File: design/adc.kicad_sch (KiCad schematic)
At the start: 26 parts, among them J6 JUMPER_DFS/GAIN, U11 TLV431ACDBZR, U12 AD9214

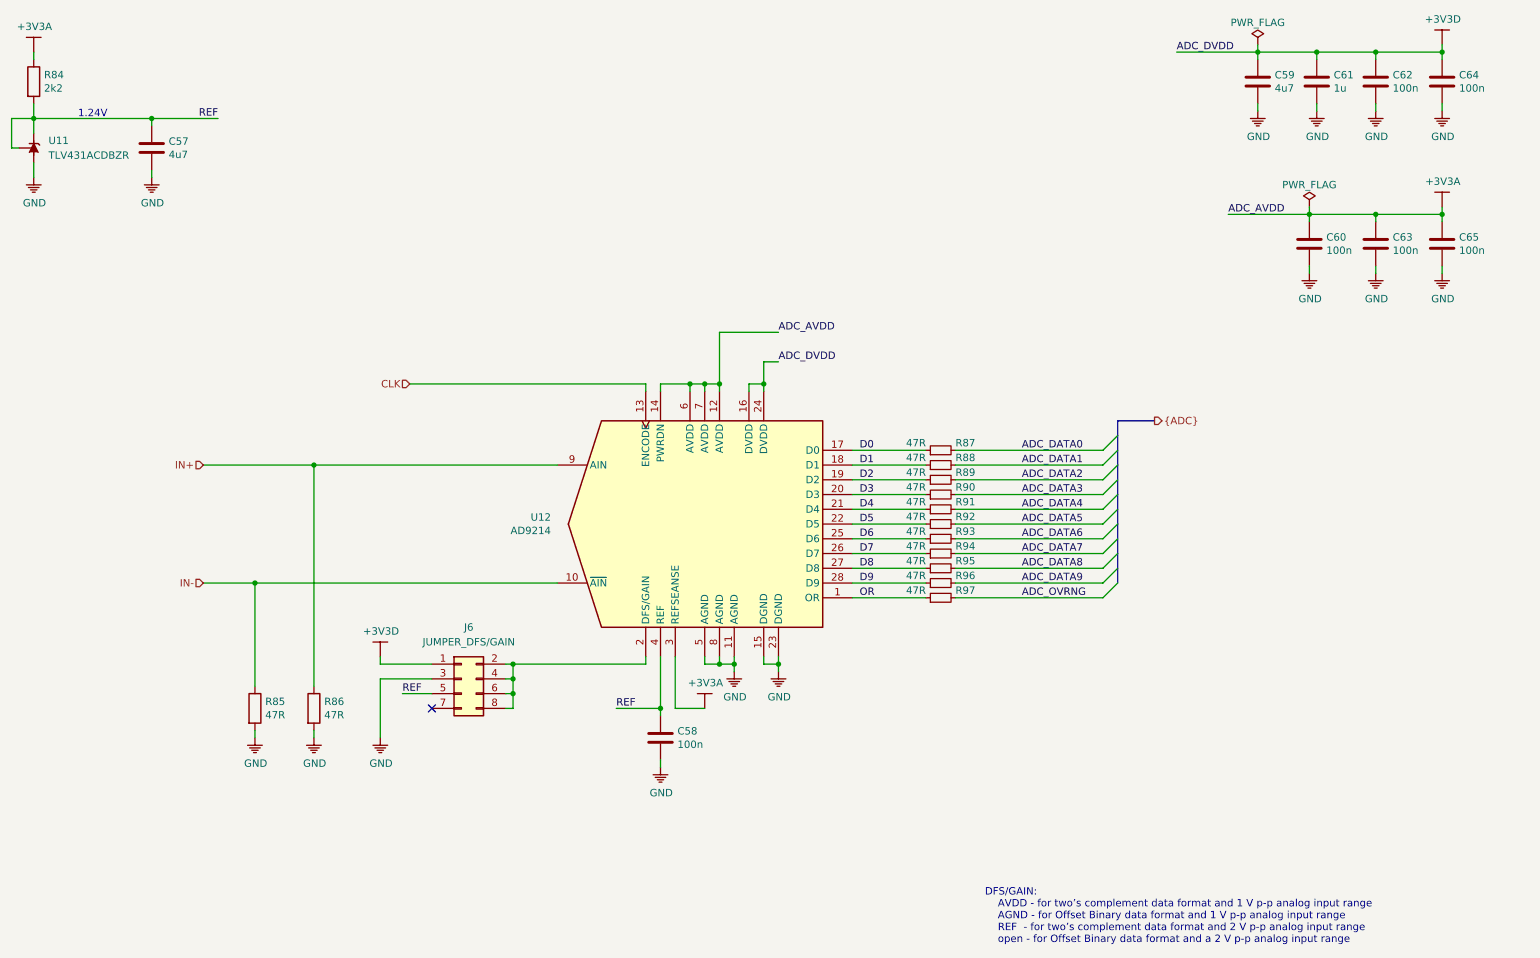
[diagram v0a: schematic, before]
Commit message: Added ADC placement
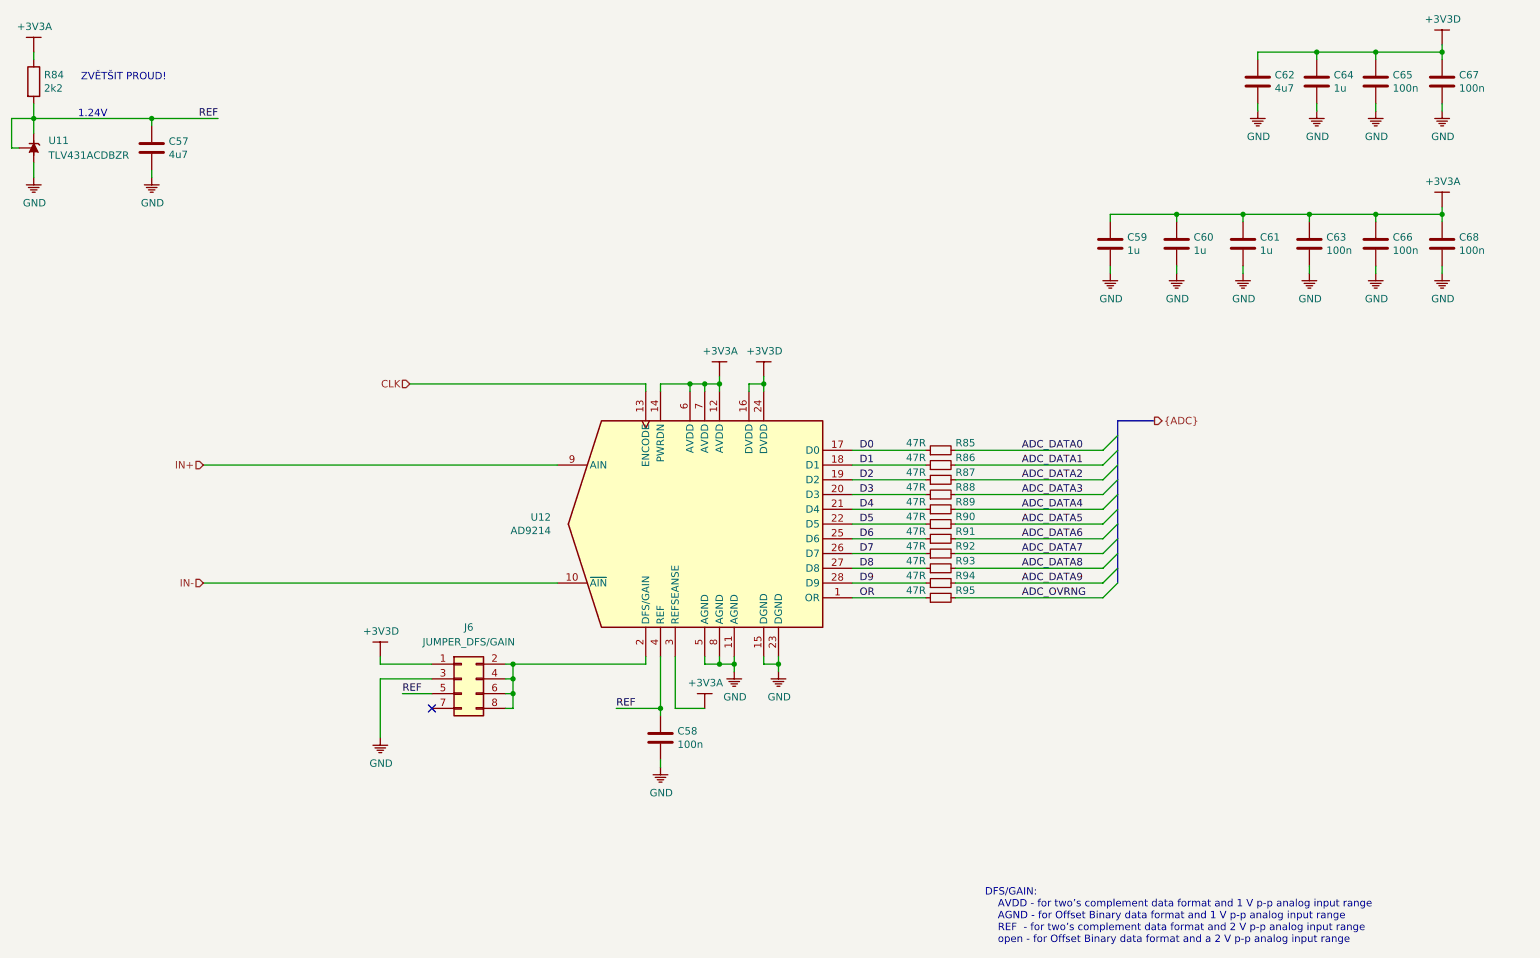
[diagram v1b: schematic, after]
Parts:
- removed R85, R86: 47R, Resistor_SMD:R_0402_1005Metric, symbol Device:R
- added C59, C60, C61: 1u, Capacitor_SMD:C_0402_1005Metric, symbol Device:C
- renumbered C59 to C62, C60 to C63, C61 to C64, C62 to C65, C63 to C66, C64 to C67, C65 to C68, R87 to R85, R88 to R86, R89 to R87, R90 to R88, R91 to R89, R92 to R90, R93 to R91, R94 to R92, R95 to R93, R96 to R94, R97 to R95
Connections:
- net +3V3A: now also C59.1, C60.1, C61.1
- net GND: now also C59.2, C60.2, C61.2
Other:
- note added: "ZVĚTŠIT PROUD!"

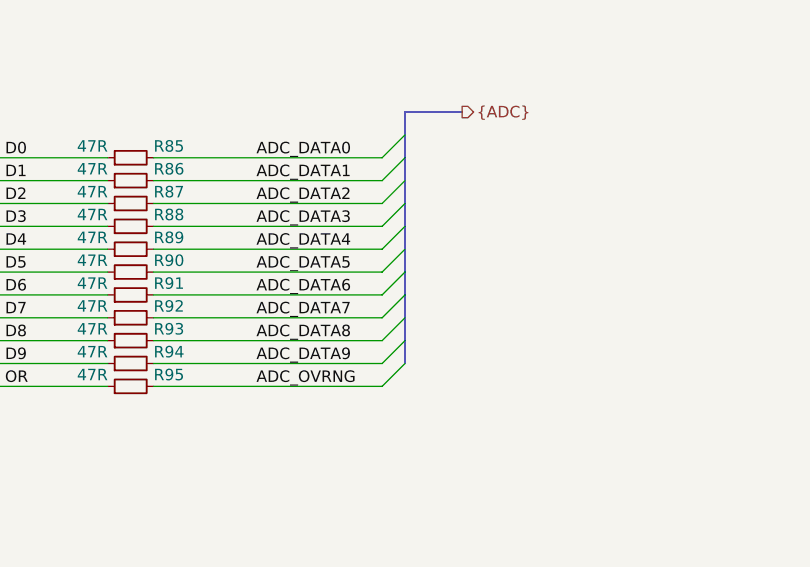
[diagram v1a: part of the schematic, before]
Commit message: Fixed LNA power
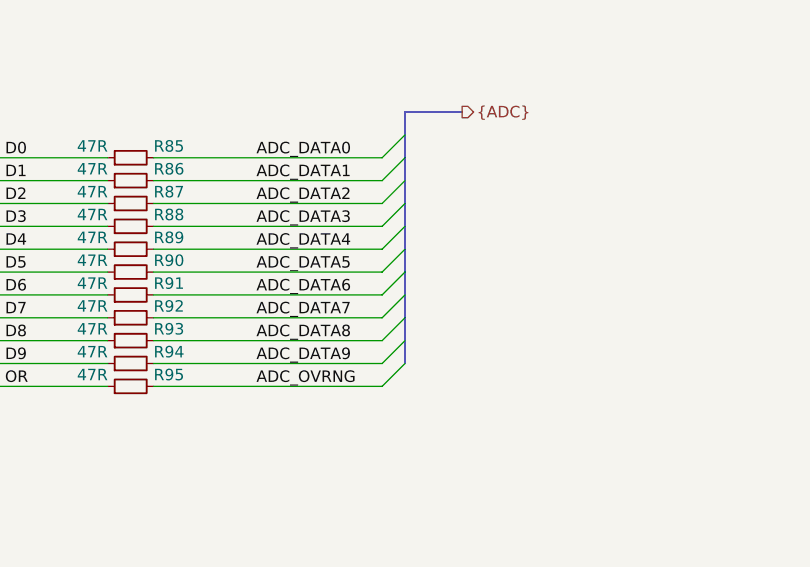
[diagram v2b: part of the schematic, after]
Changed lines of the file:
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@@
-(kicad_sch (version 20200310) (host eeschema "5.99.0-unknown-5cf474e~101~ubuntu18.04.1")
+(kicad_sch (version 20200506) (host eeschema "5.99.0-unknown-1f9723c~101~ubuntu18.04.1")
   (page "A4")
   (title_block
@@
     (company "Jan Vykydal")
   )
+  (junction (at 153.67 82.55))
+  (junction (at 110.49 130.81))
+  (junction (at 110.49 135.89))
+  (junction (at 248.92 25.4))
+  (junction (at 236.22 53.34))
+  (junction (at 148.59 130.81))
+  (junction (at 270.51 53.34))
+  (junction (at 140.97 82.55))
   (junction (at 247.65 53.34))
-  (junction (at 110.49 130.81))
+  (junction (at 27.94 36.83))
+  (junction (at 224.79 53.34))
+  (junction (at 156.21 130.81))
+  (junction (at 259.08 53.34))
+  (junction (at 135.89 138.43))
   (junction (at 48.26 36.83))
-  (junction (at 236.22 53.34))
-  (junction (at 110.49 135.89))
-  (junction (at 270.51 25.4))
-  (junction (at 224.79 53.34))
-  (junction (at 140.97 82.55))
-  (junction (at 259.08 53.34))
-  (junction (at 153.67 82.55))
   (junction (at 259.08 25.4))
-  (junction (at 143.51 82.55))
   (junction (at 146.05 82.55))
-  (junction (at 248.92 25.4))
-  (junction (at 270.51 53.34))
-  (junction (at 148.59 130.81))
   (junction (at 110.49 133.35))
   (junction (at 146.05 130.81))
-  (junction (at 27.94 36.83))
-  (junction (at 135.89 138.43))
-  (junction (at 156.21 130.81))
+  (junction (at 143.51 82.55))
+  (junction (at 270.51 25.4))
   (no_connect (at 96.52 138.43))
   (bus_entry (at 212.09 93.98) (size 2.54 -2.54))
@@
   (bus (pts (xy 214.63 88.9) (xy 214.63 93.98)))
   (bus (pts (xy 214.63 93.98) (xy 214.63 99.06)))
-  (bus (pts (xy 214.63 99.06) (xy 214.63 101.6)))
-  (bus (pts (xy 214.63 101.6) (xy 214.63 106.68)))
-  (bus (pts (xy 214.63 106.68) (xy 214.63 109.22)))
-  (bus (pts (xy 214.63 109.22) (xy 214.63 114.3)))
-  (bus (pts (xy 214.63 114.3) (xy 214.63 116.84)))
+  (bus (pts (xy 214.63 99.06) (xy 214.63 104.14)))
+  (bus (pts (xy 214.63 104.14) (xy 214.63 106.68)))
+  (bus (pts (xy 214.63 106.68) (xy 214.63 111.76)))
+  (bus (pts (xy 214.63 111.76) (xy 214.63 116.84)))
   (bus (pts (xy 220.98 88.9) (xy 214.63 88.9)))
   (text "1.24V" (at 40.64 36.83 180)

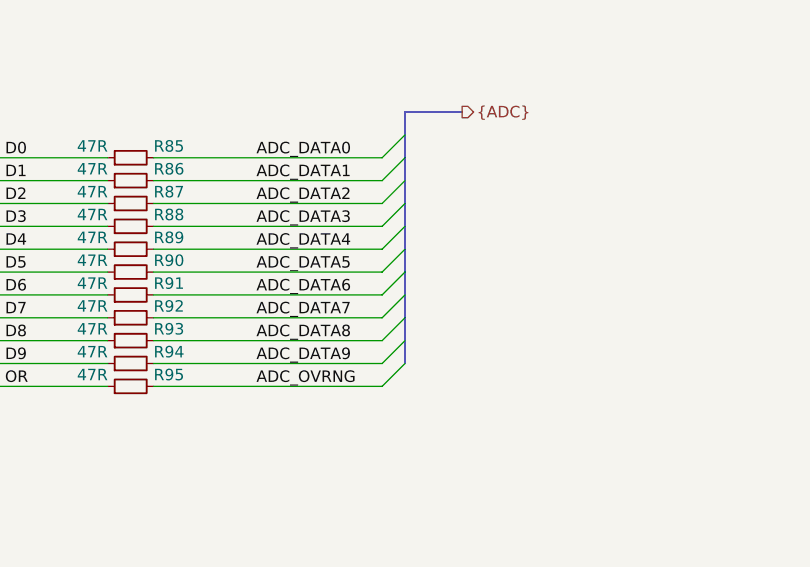
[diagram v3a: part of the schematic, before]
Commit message: Added buses that were removed when converting from the old format
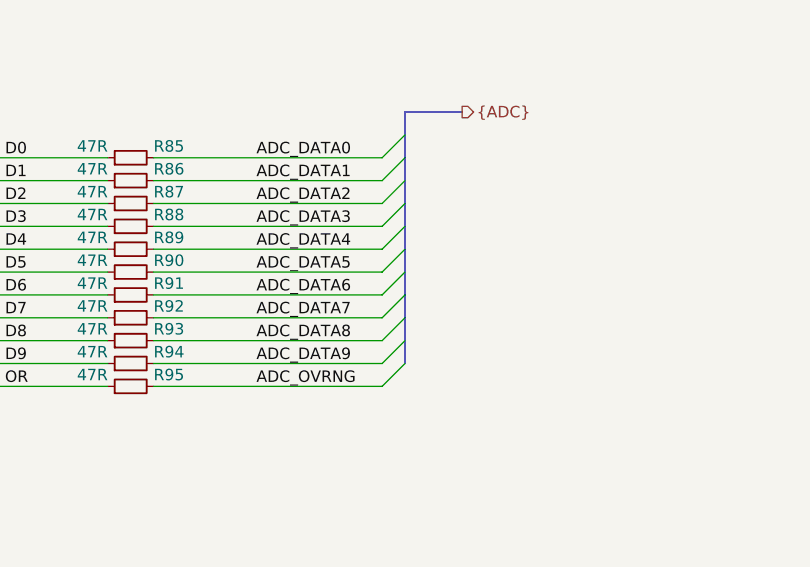
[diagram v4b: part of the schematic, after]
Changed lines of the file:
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@@
     (company "Jan Vykydal")
   )
+  (bus_alias "ADC" (members "ADC_DATA[9..0]" "ADC_OVRNG"))
+  (junction (at 146.05 82.55))
+  (junction (at 143.51 82.55))
+  (junction (at 156.21 130.81))
+  (junction (at 270.51 25.4))
+  (junction (at 146.05 130.81))
+  (junction (at 140.97 82.55))
+  (junction (at 259.08 53.34))
+  (junction (at 259.08 25.4))
+  (junction (at 110.49 130.81))
+  (junction (at 224.79 53.34))
+  (junction (at 248.92 25.4))
+  (junction (at 135.89 138.43))
+  (junction (at 48.26 36.83))
   (junction (at 153.67 82.55))
-  (junction (at 110.49 130.81))
-  (junction (at 110.49 135.89))
-  (junction (at 248.92 25.4))
   (junction (at 236.22 53.34))
   (junction (at 148.59 130.81))
+  (junction (at 247.65 53.34))
+  (junction (at 110.49 133.35))
   (junction (at 270.51 53.34))
-  (junction (at 140.97 82.55))
-  (junction (at 247.65 53.34))
+  (junction (at 110.49 135.89))
   (junction (at 27.94 36.83))
-  (junction (at 224.79 53.34))
-  (junction (at 156.21 130.81))
-  (junction (at 259.08 53.34))
-  (junction (at 135.89 138.43))
-  (junction (at 48.26 36.83))
-  (junction (at 259.08 25.4))
-  (junction (at 146.05 82.55))
-  (junction (at 110.49 133.35))
-  (junction (at 146.05 130.81))
-  (junction (at 143.51 82.55))
-  (junction (at 270.51 25.4))
   (no_connect (at 96.52 138.43))
   (bus_entry (at 212.09 93.98) (size 2.54 -2.54))
@@
   (bus (pts (xy 214.63 93.98) (xy 214.63 99.06)))
   (bus (pts (xy 214.63 99.06) (xy 214.63 104.14)))
-  (bus (pts (xy 214.63 104.14) (xy 214.63 106.68)))
-  (bus (pts (xy 214.63 106.68) (xy 214.63 111.76)))
+  (bus (pts (xy 214.63 104.14) (xy 214.63 109.22)))
+  (bus (pts (xy 214.63 109.22) (xy 214.63 111.76)))
   (bus (pts (xy 214.63 111.76) (xy 214.63 116.84)))
   (bus (pts (xy 220.98 88.9) (xy 214.63 88.9)))

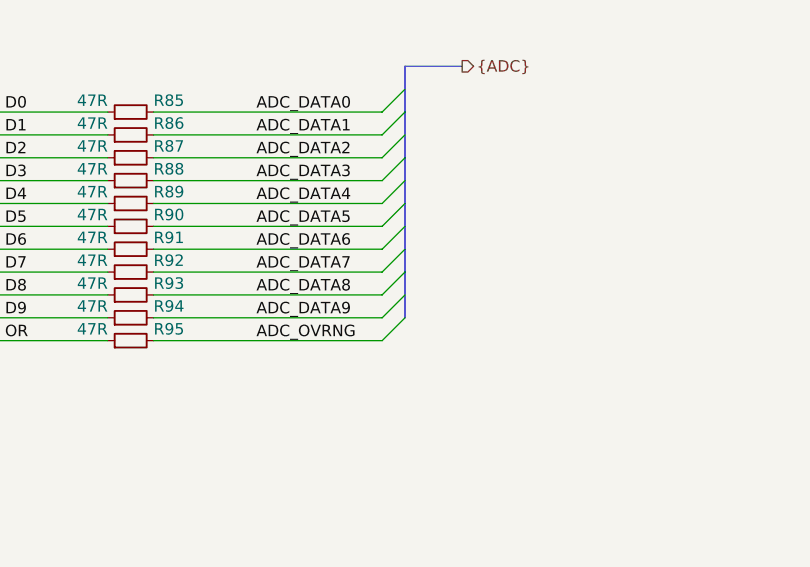
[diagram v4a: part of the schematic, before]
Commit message: Moved FPGA capacitors
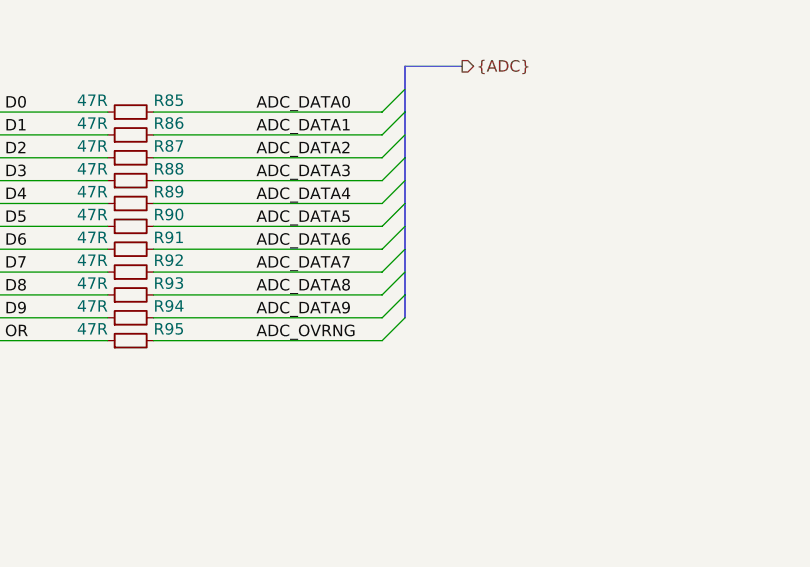
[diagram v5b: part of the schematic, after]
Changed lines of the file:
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@@
   )
   (bus_alias "ADC" (members "ADC_DATA[9..0]" "ADC_OVRNG"))
-  (junction (at 146.05 82.55))
+  (junction (at 247.65 53.34))
+  (junction (at 148.59 130.81))
   (junction (at 143.51 82.55))
-  (junction (at 156.21 130.81))
+  (junction (at 248.92 25.4))
+  (junction (at 146.05 130.81))
+  (junction (at 48.26 36.83))
+  (junction (at 270.51 53.34))
+  (junction (at 27.94 36.83))
+  (junction (at 135.89 138.43))
   (junction (at 270.51 25.4))
-  (junction (at 146.05 130.81))
+  (junction (at 110.49 133.35))
+  (junction (at 110.49 130.81))
+  (junction (at 259.08 53.34))
   (junction (at 140.97 82.55))
-  (junction (at 259.08 53.34))
-  (junction (at 259.08 25.4))
-  (junction (at 110.49 130.81))
-  (junction (at 224.79 53.34))
-  (junction (at 248.92 25.4))
-  (junction (at 135.89 138.43))
-  (junction (at 48.26 36.83))
   (junction (at 153.67 82.55))
   (junction (at 236.22 53.34))
-  (junction (at 148.59 130.81))
-  (junction (at 247.65 53.34))
-  (junction (at 110.49 133.35))
-  (junction (at 270.51 53.34))
   (junction (at 110.49 135.89))
-  (junction (at 27.94 36.83))
+  (junction (at 156.21 130.81))
+  (junction (at 224.79 53.34))
+  (junction (at 146.05 82.55))
+  (junction (at 259.08 25.4))
   (no_connect (at 96.52 138.43))
   (bus_entry (at 212.09 93.98) (size 2.54 -2.54))
@@
   (bus (pts (xy 214.63 99.06) (xy 214.63 104.14)))
   (bus (pts (xy 214.63 104.14) (xy 214.63 109.22)))
-  (bus (pts (xy 214.63 109.22) (xy 214.63 111.76)))
-  (bus (pts (xy 214.63 111.76) (xy 214.63 116.84)))
+  (bus (pts (xy 214.63 109.22) (xy 214.63 114.3)))
+  (bus (pts (xy 214.63 114.3) (xy 214.63 116.84)))
   (bus (pts (xy 220.98 88.9) (xy 214.63 88.9)))
   (text "1.24V" (at 40.64 36.83 180)

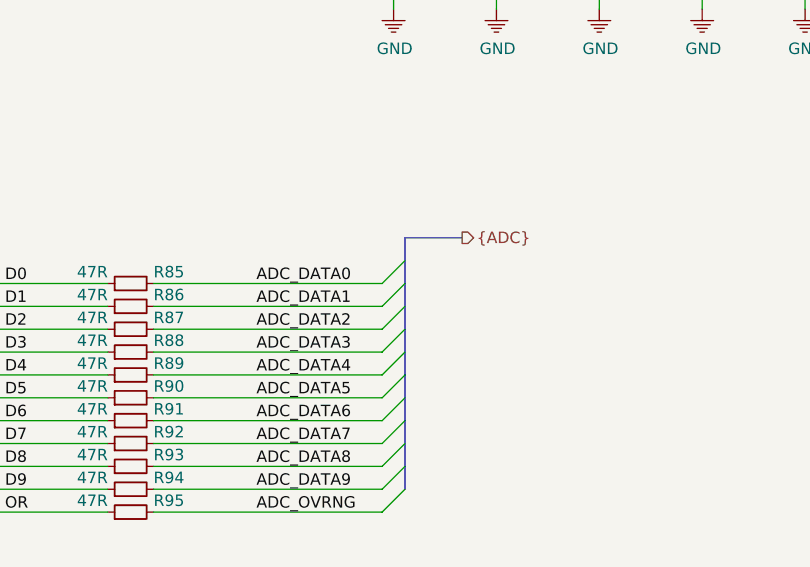
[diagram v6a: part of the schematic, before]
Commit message: Added power polygons
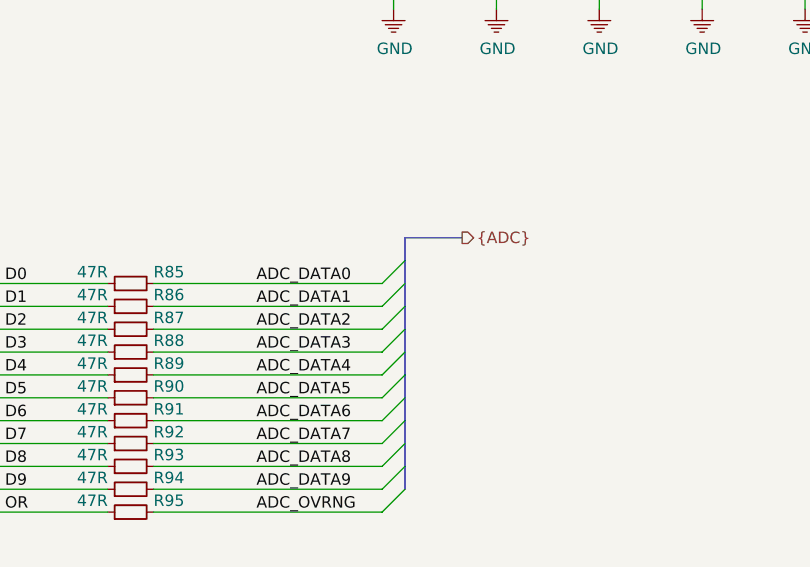
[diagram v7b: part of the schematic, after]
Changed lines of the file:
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@@
-(kicad_sch (version 20200506) (host eeschema "5.99.0-unknown-1f9723c~101~ubuntu18.04.1")
+(kicad_sch (version 20200506) (host eeschema "5.99.0-unknown-302646c~101~ubuntu18.04.1")
   (page "A4")
   (title_block
@@
   )
   (bus_alias "ADC" (members "ADC_DATA[9..0]" "ADC_OVRNG"))
+  (junction (at 248.92 25.4))
+  (junction (at 110.49 130.81))
+  (junction (at 27.94 36.83))
+  (junction (at 110.49 133.35))
+  (junction (at 135.89 138.43))
+  (junction (at 143.51 82.55))
+  (junction (at 148.59 130.81))
+  (junction (at 259.08 53.34))
+  (junction (at 236.22 53.34))
+  (junction (at 146.05 82.55))
+  (junction (at 270.51 53.34))
+  (junction (at 259.08 25.4))
+  (junction (at 110.49 135.89))
+  (junction (at 153.67 82.55))
+  (junction (at 270.51 25.4))
+  (junction (at 140.97 82.55))
   (junction (at 48.26 36.83))
-  (junction (at 259.08 25.4))
-  (junction (at 153.67 82.55))
-  (junction (at 148.59 130.81))
-  (junction (at 146.05 82.55))
-  (junction (at 110.49 133.35))
-  (junction (at 110.49 130.81))
-  (junction (at 140.97 82.55))
+  (junction (at 146.05 130.81))
+  (junction (at 247.65 53.34))
   (junction (at 156.21 130.81))
-  (junction (at 135.89 138.43))
-  (junction (at 270.51 25.4))
-  (junction (at 27.94 36.83))
-  (junction (at 236.22 53.34))
-  (junction (at 146.05 130.81))
-  (junction (at 143.51 82.55))
-  (junction (at 247.65 53.34))
-  (junction (at 259.08 53.34))
   (junction (at 224.79 53.34))
-  (junction (at 248.92 25.4))
-  (junction (at 110.49 135.89))
-  (junction (at 270.51 53.34))
   (no_connect (at 96.52 138.43))
   (bus_entry (at 212.09 93.98) (size 2.54 -2.54))
@@
   (wire (pts (xy 270.51 53.34) (xy 270.51 54.61)))
   (wire (pts (xy 270.51 62.23) (xy 270.51 63.5)))
-  (bus (pts (xy 214.63 88.9) (xy 214.63 93.98)))
-  (bus (pts (xy 214.63 93.98) (xy 214.63 99.06)))
+  (bus (pts (xy 214.63 88.9) (xy 214.63 91.44)))
+  (bus (pts (xy 214.63 91.44) (xy 214.63 96.52)))
+  (bus (pts (xy 214.63 96.52) (xy 214.63 99.06)))
   (bus (pts (xy 214.63 99.06) (xy 214.63 104.14)))
   (bus (pts (xy 214.63 104.14) (xy 214.63 109.22)))
